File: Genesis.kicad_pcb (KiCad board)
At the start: 2 copper layers, 153 x 65 mm, 36 parts, among them J1 Conn_01x02_Female, J10 Conn_01x03_Female, J11 Conn_01x04_Female, J12 Conn_01x04_Female, J13 Conn_01x02_Female, J14 Conn_01x02_Female, J15 Conn_01x08_Female, J16 Conn_01x03_Female, J17 Conn_01x01_Male, J2 Jack-DC, J3 Conn_01x06_Female, J4 Conn_01x06_Female, J5 Conn_01x05_Female, J6 Conn_01x01_Male, J7 Conn_01x03_Female, J8 Conn_01x08_Female, J9 Conn_01x03_Female, K1 SANYOU_SRD_Form_C, K2 SANYOU_SRD_Form_C, Q1 2N2219, Q2 2N2219, U1 LM7805_TO220

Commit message: Corrijo error de MP3
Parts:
- moved J8 17.8 mm to (198.0, 86.8), turned to 180 degrees
- moved J10 6.48 mm to (129.0, 66.6)
- moved J9 6.48 mm to (129.0, 56.1)
- moved U1 4.46 mm to (105.5, 56.5)
- moved J1 2.15 mm to (198.0, 94.3), turned to 0 degrees
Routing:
- net Net-(J1-Pad2): track 7.18 -> 33.3 mm
- net +5V: track 476.4 -> 454.7 mm
- net /RX_MP3: track 12.2 -> 24.3 mm
- net GND: track 167.2 -> 156.4 mm
- net /TX_MP3: track 53.8 -> 64.2 mm
- net Net-(J1-Pad1): track 16.2 -> 25.7 mm
- net Net-(A1-Pad20): track 25.2 -> 18.7 mm
- net Net-(A1-Pad19): track 23.9 -> 18.3 mm
- net +12V: track 94.4 -> 98.8 mm

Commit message: Agrego modulo conector de chip GSM Quectel M10
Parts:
- moved J15 18.9 mm to (200.4, 69.9), turned to 270 degrees
- moved J8 15.4 mm to (182.6, 86.4), turned to 90 degrees
- moved C1 2.34 mm to (77.7, 58.3)
- moved C2 2.34 mm to (89.7, 58.3)
- moved C3 2.34 mm to (83.7, 58.5)
- moved U1 1.34 mm to (104.1, 56.5)
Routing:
- net Net-(J1-Pad2): track 33.3 -> 12.2 mm
- net GND: track 156.4 -> 139.4 mm
- net Net-(J1-Pad1): track 25.7 -> 9.22 mm
- net /RX_MP3: track 24.3 -> 38.3 mm
- net /TX_MP3: track 64.2 -> 76.9 mm
- net +5V: track 454.7 -> 444.1 mm
- net Net-(J3-Pad4): track 46.1 -> 41.0 mm
- net Net-(A1-Pad9): track 32.1 -> 29.4 mm
- net /SDA: track 56.3 -> 53.7 mm
- net Net-(A1-Pad13): track 25.0 -> 22.8 mm
- net Net-(A1-Pad14): track 21.6 -> 19.5 mm
- net +12V: track 98.8 -> 97.4 mm
- net Net-(A1-Pad12): track 28.4 -> 27.1 mm
- net +3V3: track 59.9 -> 58.7 mm
- net Net-(A1-Pad15): track 17.4 -> 16.3 mm
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
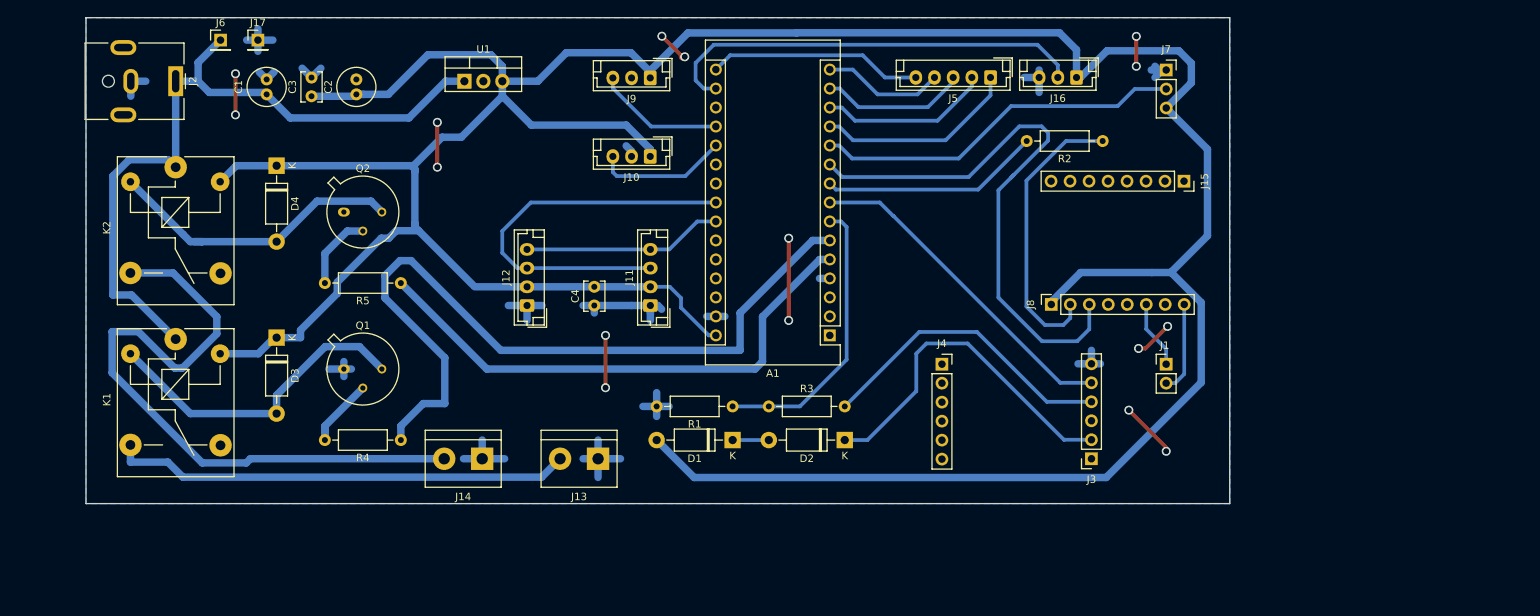
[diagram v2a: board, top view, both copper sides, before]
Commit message: Incluyo BC66 en la misma placa
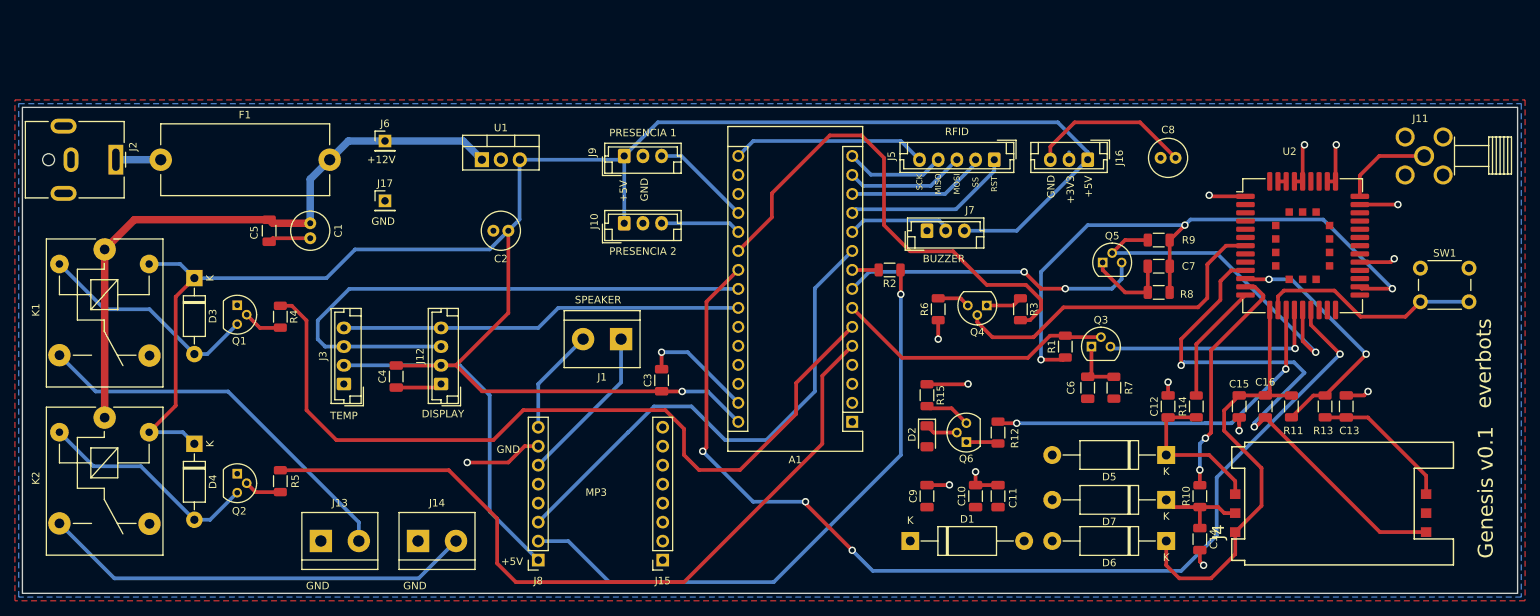
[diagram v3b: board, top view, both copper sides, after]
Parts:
- added C10: 100p, Capacitor_SMD:C_1206_3216Metric, F.Cu at (172.5, 112.0)
- added C11: 22p, Capacitor_SMD:C_1206_3216Metric, F.Cu at (175.5, 112.0)
- added C12: 33p, Capacitor_SMD:C_1206_3216Metric, F.Cu at (198.2, 100.0)
- added C13: 33p, Capacitor_SMD:C_1206_3216Metric, F.Cu at (222.1, 100.0)
- added C14: 33p, Capacitor_SMD:C_1206_3216Metric, F.Cu at (202.5, 117.8)
- added C15: 33p, Capacitor_SMD:C_1206_3216Metric, F.Cu at (207.8, 100.0)
- added C16: 100n, Capacitor_SMD:C_1206_3216Metric, F.Cu at (211.2, 100.0)
- added C5: 220n, Capacitor_SMD:C_1206_3216Metric, F.Cu at (78.0, 76.5)
- added C6: 1n, Capacitor_SMD:C_1206_3216Metric, F.Cu at (187.5, 97.5)
- added C7: 1n, Capacitor_SMD:C_1206_3216Metric, F.Cu at (197.0, 81.2)
- added C8: 100u, Capacitor_THT:C_Radial_D5.0mm_H11.0mm_P2.00mm, F.Cu at (197.2, 66.8)
- added C9: 100n, Capacitor_SMD:C_1206_3216Metric, F.Cu at (166.0, 112.0)
- added D5: P6KE12A, Diode_THT:D_DO-15_P15.24mm_Horizontal, F.Cu at (198.0, 106.5)
- added D6: P6KE12A, Diode_THT:D_DO-15_P15.24mm_Horizontal, F.Cu at (198.0, 118.0)
- added D7: P6KE12A, Diode_THT:D_DO-15_P15.24mm_Horizontal, F.Cu at (198.0, 112.5)
- added F1: Fuse, Fuse:Fuseholder_Cylinder-5x20mm_Stelvio-Kontek_PTF78_Horizontal_Open, F.Cu at (63.5, 67.0)
- added Q3: BC546, Package_TO_SOT_THT:TO-92, F.Cu at (188.0, 92.0)
- added Q4: BC546, Package_TO_SOT_THT:TO-92, F.Cu at (174.0, 86.5)
- added Q5: BC546, Package_TO_SOT_THT:TO-92, F.Cu at (189.5, 80.8)
- added Q6: BC546, Package_TO_SOT_THT:TO-92, F.Cu at (171.3, 104.8)
- added R10: 22, Resistor_SMD:R_1206_3216Metric, F.Cu at (202.5, 112.0)
- added R11: 10k, Resistor_SMD:R_1206_3216Metric, F.Cu at (214.8, 100.0)
- added R12: 4.7k, Resistor_SMD:R_1206_3216Metric, F.Cu at (175.5, 103.5)
- added R13: 22, Resistor_SMD:R_1206_3216Metric, F.Cu at (219.2, 100.0)
- added R14: 22, Resistor_SMD:R_1206_3216Metric, F.Cu at (202.0, 100.0)
- added R15: 47k, Resistor_SMD:R_1206_3216Metric, F.Cu at (166.0, 98.5)
- added R6: 47k, Resistor_SMD:R_1206_3216Metric, F.Cu at (167.5, 87.0)
- added R7: 4.7k, Resistor_SMD:R_1206_3216Metric, F.Cu at (191.0, 97.5)
- added R8: 4.7k, Resistor_SMD:R_1206_3216Metric, F.Cu at (197.0, 84.8)
- added R9: 10k, Resistor_SMD:R_1206_3216Metric, F.Cu at (197.0, 77.8)
- added SW1: SW_Push, Button_Switch_THT:SW_PUSH_6mm_H5mm, F.Cu at (232.0, 81.5)
- added U2: BC66, RF_GSM:Quectel_BC66, F.Cu at (216.2, 78.5)
- C1: value 0.33u -> 10u
- C2: value 100u -> 1u
- C3, C4: value 0.1u -> 100n; footprint Capacitor_THT:C_Disc_D3.8mm_W2.6mm_P2.50mm -> Capacitor_SMD:C_1206_3216Metric
- D1: value 1N4007 -> P6KE12A; footprint Diode_THT:D_DO-41_SOD81_P10.16mm_Horizontal -> Diode_THT:D_DO-15_P15.24mm_Horizontal
- D2: value 1N4007 -> LED_RED; footprint Diode_THT:D_DO-41_SOD81_P10.16mm_Horizontal -> LED_SMD:LED_1206_3216Metric
- D3, D4: value 1N4004 -> 1N4007
- J1: value Conn_01x02_Female -> Conn_01x02; footprint Connector_PinHeader_2.54mm:PinHeader_1x02_P2.54mm_Vertical -> TerminalBlock:TerminalBlock_bornier-2_P5.08mm
- J10, J16, J9: value Conn_01x03_Female -> Conn_01x03
- J11: value Conn_01x04_Female -> SMA; footprint Connector_JST:JST_EH_B4B-EH-A_1x04_P2.50mm_Vertical -> Libreria:TE_221790-1
- J12: value Conn_01x04_Female -> Conn_01x04
- J13, J14: value Conn_01x02_Female -> Conn_01x02
- J15, J8: value Conn_01x08_Female -> Conn_01x08
- J17, J6: value Conn_01x01_Male -> Conn_01x01
- J3: value Conn_01x06_Female -> Conn_01x04; footprint Connector_PinSocket_2.54mm:PinSocket_1x06_P2.54mm_Vertical -> Connector_JST:JST_EH_B4B-EH-A_1x04_P2.50mm_Vertical
- J4: value Conn_01x06_Female -> SIM; footprint Connector_PinSocket_2.54mm:PinSocket_1x06_P2.54mm_Vertical -> SnapEDA Library:GCT_SIM5060-6-0-26-00-X_REVC
- J5: value Conn_01x05_Female -> Conn_01x05
- J7: value Conn_01x03_Female -> Conn_01x03; footprint Connector_PinSocket_2.54mm:PinSocket_1x03_P2.54mm_Vertical -> Connector_JST:JST_EH_B3B-EH-A_1x03_P2.50mm_Vertical
- Q1, Q2: value 2N2219 -> BC547; footprint Package_TO_SOT_THT:TO-39-3 -> Package_TO_SOT_THT:TO-92
- R1: value 1k -> 10k; footprint Resistor_THT:R_Axial_DIN0207_L6.3mm_D2.5mm_P10.16mm_Horizontal -> Resistor_SMD:R_1206_3216Metric
- R2, R4, R5: footprint Resistor_THT:R_Axial_DIN0207_L6.3mm_D2.5mm_P10.16mm_Horizontal -> Resistor_SMD:R_1206_3216Metric
- R3: value 1k -> 4.7k; footprint Resistor_THT:R_Axial_DIN0207_L6.3mm_D2.5mm_P10.16mm_Horizontal -> Resistor_SMD:R_1206_3216Metric
- moved J11 105.4 mm to (232.5, 66.5), turned to 0 degrees
- moved J3 100.5 mm to (88.0, 97.0), turned to 90 degrees
- moved J15 86.2 mm to (130.7, 120.6), turned to 180 degrees
- moved J8 76.7 mm to (114.0, 120.6), turned to 180 degrees
- moved J1 73.0 mm to (125.1, 91.0), turned to 180 degrees
- moved C3 60.3 mm to (130.5, 96.5)
- moved J4 55.2 mm to (220.0, 113.0), turned to 90 degrees
- moved R1 45.2 mm to (184.5, 92.0), turned to 90 degrees
- moved D4 38.8 mm to (68.0, 105.0)
- moved J13 38.7 mm to (84.9, 118.0), turned to 0 degrees
- moved J7 38.6 mm to (166.0, 76.5)
- moved Q2 37.8 mm to (73.7, 109.0), turned to 270 degrees
- moved R3 36.1 mm to (178.5, 87.0), turned to 270 degrees
- moved K2 34.8 mm to (56.0, 101.5)
- moved R2 33.3 mm to (161.0, 81.8)
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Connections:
- net Net-(A1-Pad11) renamed /Buzzer
- net Net-(A1-Pad12) renamed /RST
- net Net-(A1-Pad13) renamed /SS
- net Net-(A1-Pad14) renamed /MOSI
- net Net-(A1-Pad15) renamed /MISO
- net Net-(A1-Pad16) renamed /SCK
- net Net-(A1-Pad19) renamed /Sensor_presencia2
- net Net-(A1-Pad20) renamed /Sensor_presencia1
- A1 pad 21: Net-(A1-Pad21) -> /PWR_KEY
- A1 pad 22: Net-(A1-Pad22) -> /PSM_EINT
- A1 pad 9: Net-(A1-Pad9) -> /RX_MP3
- D1 pad 1: Net-(D1-Pad1) -> +3V3
- D1 pad 2: +5V -> GND
- D2 pad 2: Net-(D1-Pad1) -> +3V3
- J11 pad 1: GND -> Net-(J11-Pad1)
- J11 pad 2: +5V -> GND
- J11 pad 3: /SDA -> GND
- J11 pad 4: /SCL -> GND
- J2 pad 1: +12V -> Net-(F1-Pad1)
- J3 pad 1: Net-(J3-Pad1) -> GND
- J3 pad 2: Net-(D2-Pad1) -> +5V
- J3 pad 3: Net-(J3-Pad3) -> /SDA
- J3 pad 4: Net-(J3-Pad4) -> /SCL
- J8 pad 2: /RX_MP3 -> Net-(J8-Pad2)
- R1 pad 1: /RXD_GSM -> /Quectel_BC66/VDD_EXT
- R1 pad 2: GND -> /RXD_GSM
- R2 pad 1: /RX_MP3 -> Net-(J8-Pad2)
- R2 pad 2: Net-(A1-Pad9) -> /RX_MP3
- R3 pad 1: /RXD_GSM -> Net-(Q4-Pad1)
- R3 pad 2: Net-(J3-Pad4) -> /PWR_KEY
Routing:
- net /PSM_EINT: track 0.00 -> 142.3 mm, vias 0 -> 4
- net +5V: track 444.1 -> 317.2 mm, vias 0 -> 1
- net /Quectel_BC66/VDD_EXT: track 0.00 -> 83.2 mm, vias 0 -> 3
- net Net-(J8-Pad2): track 0.00 -> 82.6 mm, vias 0 -> 1
- net Net-(C16-Pad2): track 0.00 -> 74.5 mm, vias 0 -> 2
- net /PWR_KEY: track 0.00 -> 67.8 mm
- net Net-(C15-Pad1): track 0.00 -> 58.8 mm
- net +3V3: track 58.7 -> 2.10 mm
- net Net-(R12-Pad2): track 0.00 -> 50.3 mm, vias 0 -> 2
- net Net-(Q4-Pad2): track 0.00 -> 45.4 mm
- net Net-(Q5-Pad2): track 0.00 -> 44.7 mm, vias 0 -> 1
- net Net-(D2-Pad1): track 46.6 -> 4.37 mm
- net Net-(J3-Pad4): track 41.0 -> 0.00 mm
- net Net-(J14-Pad2): track 94.3 -> 58.2 mm
- net /Buzzer: track 49.6 -> 14.0 mm
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- added copper zone on F.Cu, net +3V3
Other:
- board size 153 x 65 mm -> 200 x 65 mm
- net class Default: clearance 0.3556 -> 0.15; trace_width 0.3048 -> 0.25; via_dia 1.2 -> 0.25; via_drill 0.8 -> 0.2
- rule trace_clearance: 0.3556 -> 0.15
- rule via_min_drill: 0.3 -> 0.2
- rule via_min_size: 0.4 -> 0.25
- board text added: "+12V"
- board text added: "+3V3"
- board text added: "+5V"
- board text added: "BUZZER"
- board text added: "DISPLAY"
- board text added: "GND"
- board text added: "Genesis v0.1"
- board text added: "MISO"
- board text added: "MOSI"
- board text added: "MP3"
- board text added: "PRESENCIA 1"
- board text added: "PRESENCIA 2"
- board text added: "RFID"
- board text added: "RST"
- board text added: "SCK"
- board text added: "SPEAKER"
- board text added: "SS"
- board text added: "TEMP"
- board text added: "everbots"
